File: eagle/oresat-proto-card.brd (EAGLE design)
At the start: 99.8 x 94.7 mm, 114 parts, among them J1 J-SAMTEC-TFM-110-X1-XXX-D-RA, J2 U.FL, J3 U.FL, J4 U.FL, J6 J-SAMTEC-TFM-120-X1-XXX-D-RA, J7 FTSH-105-XX-X-DV-K, Q1 DMP2240UDM, Q3 MOSFET-PCH-SOT23-6, Q4 MOSFET-PCH-SOT23-6, Q5 PMV45EN, Q6 PMV45EN, U2 TCAN330, U3 MAX7310ATE, U4 MAX4211CETE, U5 TPS62111RSA, U6 STM32F042K6, U7 MCP1703A, X1 16MHZ-2.5x2mm

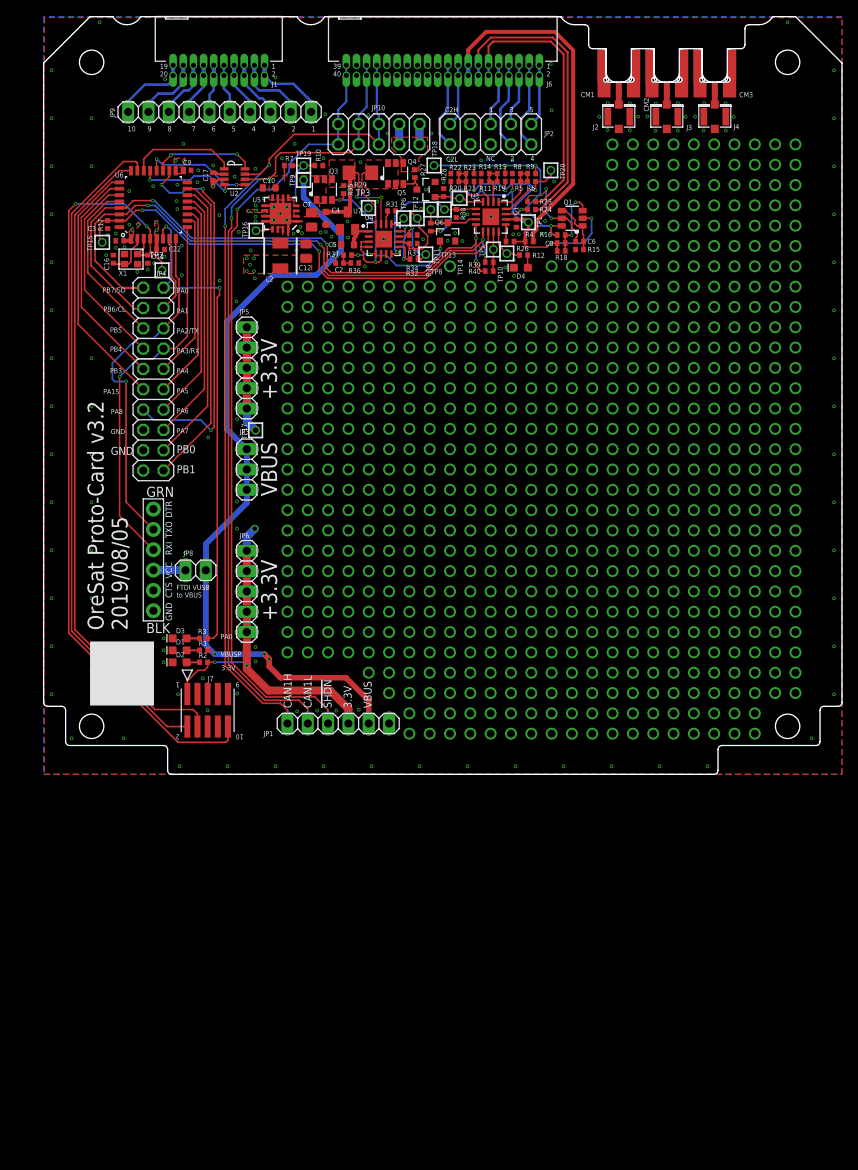
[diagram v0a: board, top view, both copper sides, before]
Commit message: updates to OPD, new I2C protection circuit
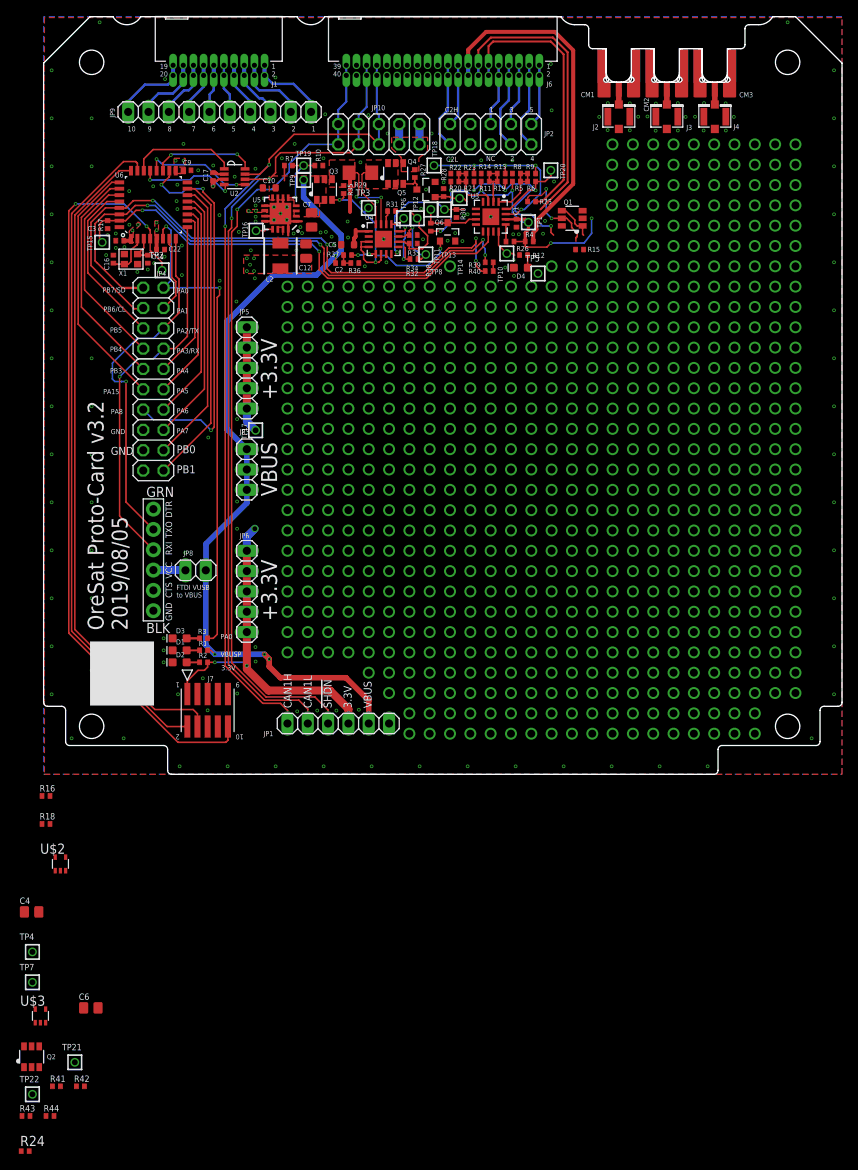
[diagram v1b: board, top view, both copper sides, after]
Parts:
- removed C8: TBD, rcl_custom:.0402-B-NOSILK
- removed U7: MCP1703A, v-reg:SOT23
- added Q2: DMP2240UDM, Q-MOSFET-PCH-dual-SOT23-6:SOT23-6
- added R41: 100, rcl_custom:.0402-B-NOSILK
- added R42: 10k, rcl_custom:.0402-B-NOSILK
- added R43, R44: NP, rcl_custom:.0402-B-NOSILK
- added TP21, TP22, TP4, TP7: TEST-POINT, Tova:2MM-TEST-POINT
- added U$2, U$3: MIC842, Q-Microchip-MIC842-Comparator:SC70-5
- C4: value 1u -> NP; device oresat-rcl:.0603-B-NOSILK -> oresat-rcl:.0805-B-NOSILK
- C6: value TBD -> NP; device rcl_custom:.0402-B-NOSILK -> oresat-rcl:.0805-B-NOSILK
- R16, R18: value 10k -> NP
- R24: value 100 -> 10k; device rcl_custom:.0402-B-NOSILK -> rcl:R0402
- moved R24 133.6 mm to (-2.30, -47.1), turned to 0 degrees
- moved C6 113.6 mm to (5.90, -29.2)
- moved R18 96.3 mm to (0.30, -6.20), turned to 0 degrees
- moved R16 95.2 mm to (0.30, -2.70)
- moved C4 94.2 mm to (-1.50, -17.2), turned to 0 degrees
- moved TP5 6.33 mm to (61.8, 62.6)
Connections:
- net BOOT renamed BOOT0
- removed net N$573: R12.2, TP10.1, U3.12
- removed net N$581: C8.2, Q1.3, R16.2, R18.1
- removed net N$598: R31.2, U4.14
- removed net N$600: TP6.1, U4.13
- removed net PA15: JP4.11, U6.25
- removed net PA8: JP4.13, U6.18
- new net IOUT: JP4.11, R31.2, U4.14, U6.25
- new net N$479: Q2.5, R41.2
- new net N$480: Q2.1, R42.2, TP22.1, U$3.5
- new net POUT: R24.1, TP6.1, U4.13
- new net POUTNAM: JP4.13, R24.2, U6.18
- net CB-RESET: now also U3.9, U4.9; no longer U3.5, U4.8
- net GND: now also C6.2, R42.1, U$2.2, U$3.2; no longer U7.1
- net MAX4211-3V3: now also TP10.1, U3.12; no longer U7.2
- net N$398: no longer C4.1, U7.3
- net N$579: no longer C6.1
- net N$580: now also TP7.1, U$2.5; no longer C6.2, Q1.4
- net N$599: now also U4.8; no longer U4.9
- net ON/!OFF: now also R12.2, U3.8; no longer U3.4
- net OPD_SCL: now also R41.1; no longer R24.1
- net PB6/SCL: now also U3.4; no longer U3.8
- net PB7/SDA: now also U3.5; no longer U3.9
- net PEN-SCL-FILT: now also C6.1, Q2.6, R43.1, R43.2, R44.1, TP21.1, U$3.1; no longer R24.2
- net PEN-SDA-FILT: now also C4.1, R16.2, R18.1, TP4.1, U$2.1
- net VPD: now also R44.2, U$2.4, U$3.4; no longer C8.1, Q1.2
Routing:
- net POUTNAM: track 0.00 -> 48.5 mm, vias 0 -> 3
- net PA8: track 48.5 -> 0.00 mm, vias 3 -> 0
- net IOUT: track 0.00 -> 33.6 mm
- net PA15: track 31.9 -> 0.00 mm
- net N$581: track 8.81 -> 0.00 mm, vias 2 -> 0
- net N$573: track 4.85 -> 0.00 mm
- net MAX4211-3V3: track 3.79 -> 7.65 mm
- net N$385: track 4.95 -> 1.14 mm
- net N$398: track 18.6 -> 15.6 mm
- net VPD: track 46.0 -> 43.1 mm
- net N$580: track 6.65 -> 4.40 mm
- net ON/!OFF: track 6.27 -> 4.28 mm
- net CB-RESET: track 16.7 -> 14.8 mm
- net POUT: track 0.00 -> 1.83 mm
- net N$600: track 1.83 -> 0.00 mm
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
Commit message: added board layout of new I2C protection circuit
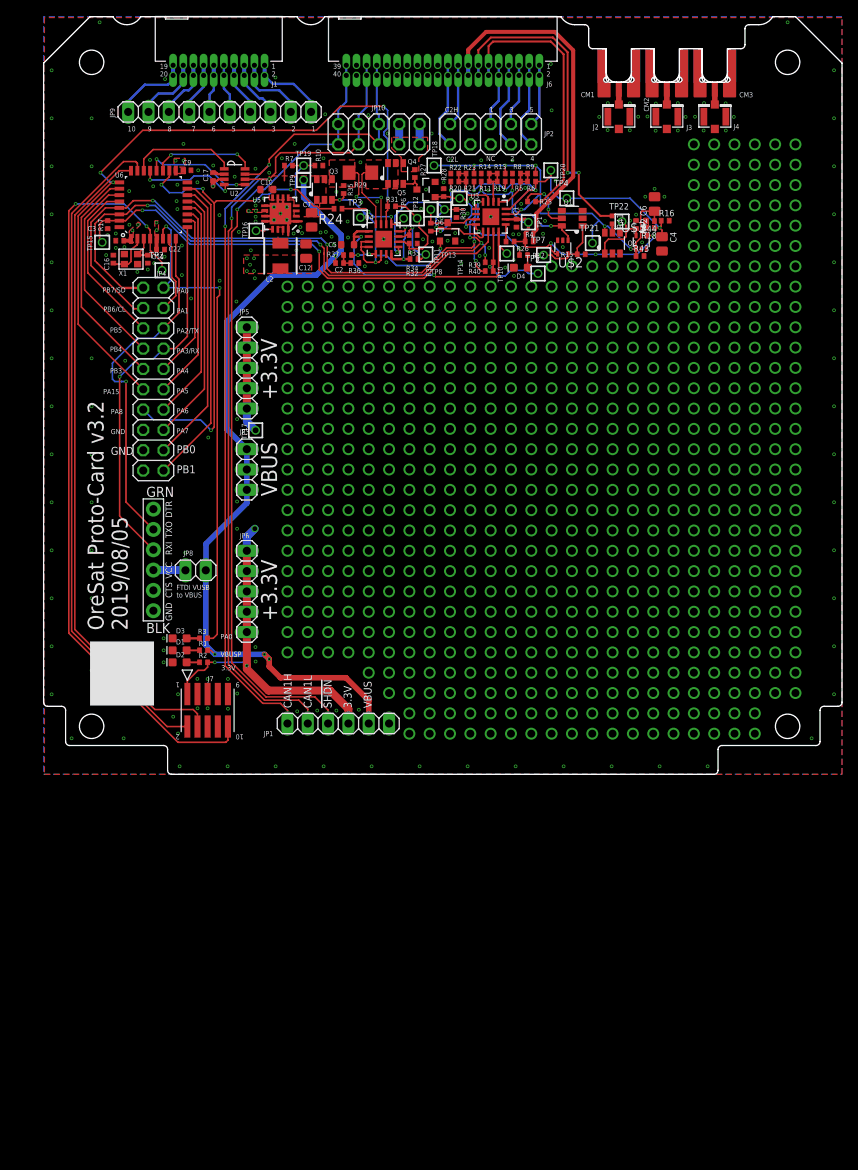
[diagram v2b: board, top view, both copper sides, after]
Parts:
- moved R44 134.7 mm to (75.8, 69.2), turned to 180 degrees
- moved R43 132.1 mm to (74.5, 64.8)
- moved TP22 131.7 mm to (72.3, 69.1)
- moved R41 128.7 mm to (71.1, 69.3), turned to 270 degrees
- moved R42 128.2 mm to (74.1, 68.7), turned to 270 degrees
- moved Q2 125.0 mm to (71.1, 66.4)
- moved R24 124.1 mm to (36.8, 70.7), turned to 180 degrees
- moved C6 122.7 mm to (76.4, 71.3), turned to 90 degrees
- moved U$3 122.4 mm to (74.7, 66.5)
- moved TP21 121.1 mm to (68.6, 66.4)
- moved TP4 115.5 mm to (65.4, 72.0)
- moved C4 114.8 mm to (77.3, 66.3), turned to 270 degrees
- moved TP7 111.1 mm to (62.5, 64.9)
- moved R18 106.1 mm to (75.8, 68.3), turned to 180 degrees
- moved R16 105.6 mm to (77.7, 69.2)
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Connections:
- net POUTNAM renamed POUTPROT
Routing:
- net IOUT: track 33.6 -> 88.3 mm, vias 0 -> 4
- net PEN-SCL-FILT: track 24.9 -> 53.9 mm, vias 4 -> 6
- net MAX4211-3V3: track 7.65 -> 35.4 mm, vias 0 -> 2
- net PEN-SDA-FILT: track 30.4 -> 53.8 mm, vias 4 -> 5
- net POUTPROT: track 48.5 -> 65.2 mm, vias 3 -> 5
- net ON/!OFF: track 4.28 -> 17.2 mm, vias 0 -> 4
- net N$385: track 1.14 -> 12.3 mm, vias 0 -> 1
- net CB-RESET: track 14.8 -> 24.8 mm, vias 1 -> 2
- net VPD: track 43.1 -> 52.5 mm, vias 6 -> 7
- net N$480: track 0.00 -> 8.94 mm
- net POUT: track 1.83 -> 9.34 mm, vias 0 -> 2
- net PB7/SDA: track 71.6 -> 78.1 mm, vias 4 -> 6
- net N$579: track 12.7 -> 7.44 mm
- net PB6/SCL: track 76.0 -> 80.9 mm, vias 4 -> 5
- net N$398: track 15.6 -> 10.7 mm
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- added copper zone on layer 1, net VPD

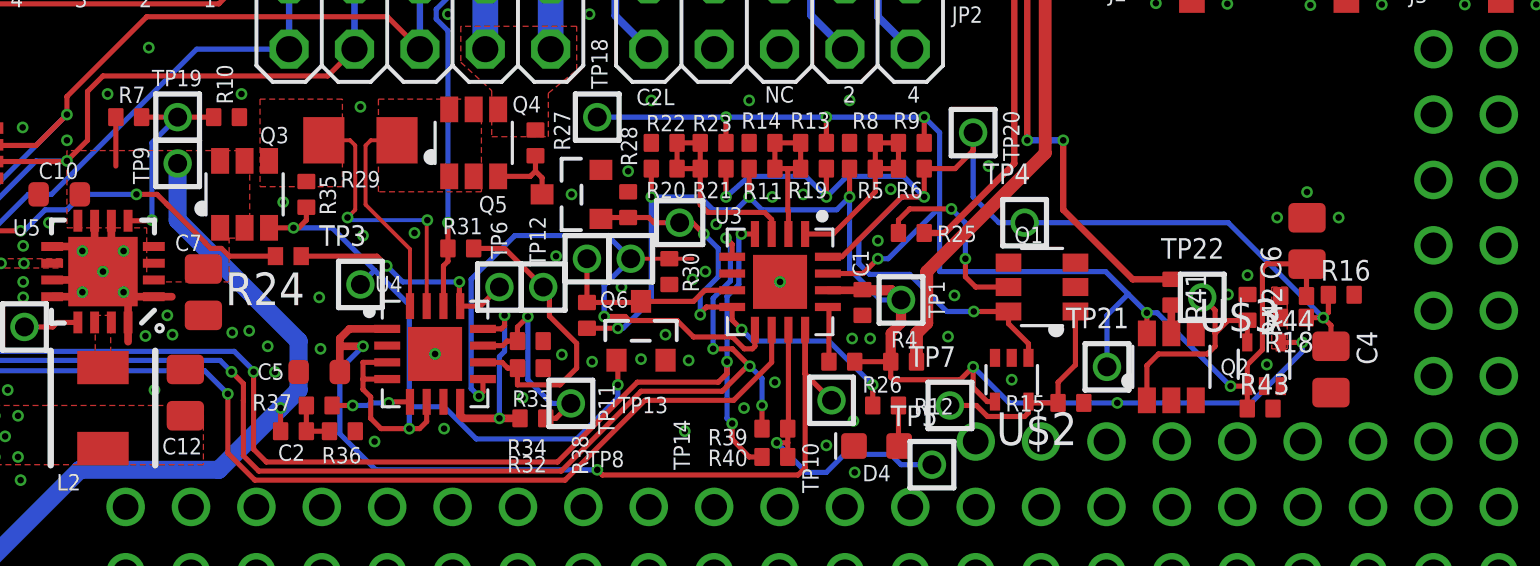
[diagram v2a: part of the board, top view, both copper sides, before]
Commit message: stray airwire
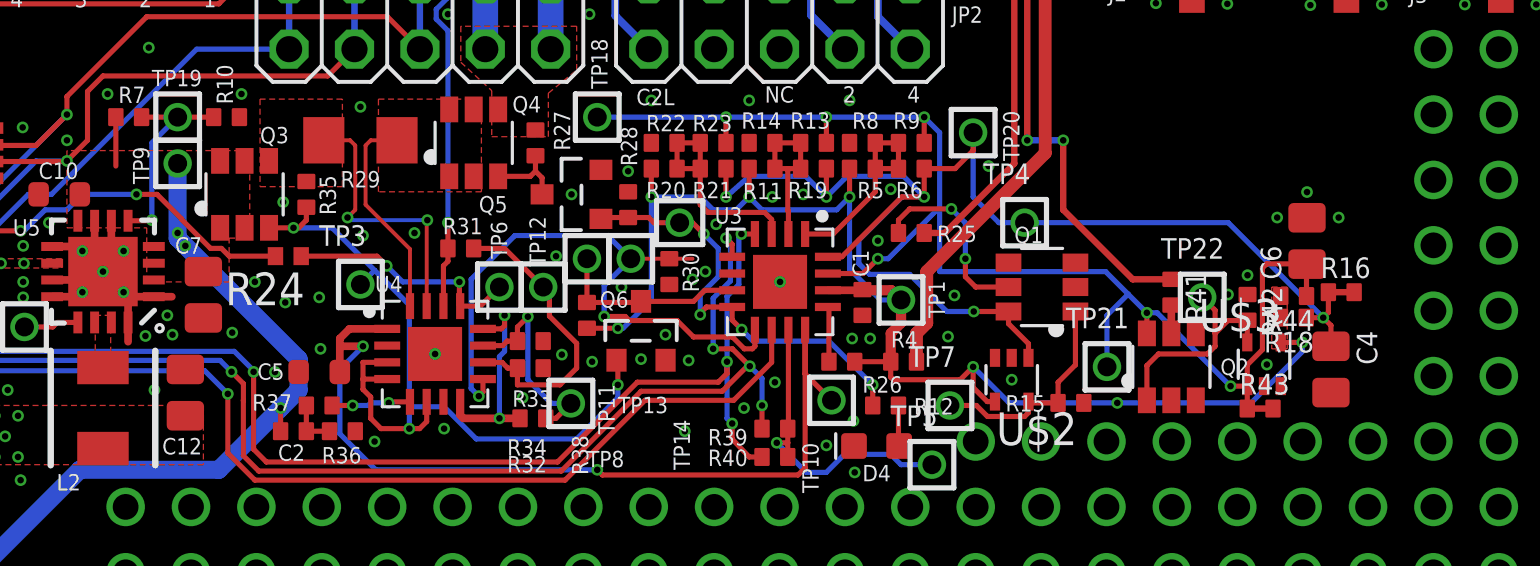
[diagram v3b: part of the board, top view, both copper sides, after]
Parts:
- moved C7 0.10 mm to (33.5, 69.2)
- moved R16 0.10 mm to (77.7, 69.3)
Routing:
- net PEN-SDA-FILT: track 53.8 -> 54.9 mm
- net PEN-SCL-FILT: track 53.9 -> 54.9 mm
- net VBUSP: vias 4 -> 6
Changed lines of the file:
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@@
 <attribute name="NAME" x="31.5" y="77.3" size="0.635" layer="25" font="vector" ratio="20"/>
 </element>
-<element name="C7" library="oresat-rcl" package=".0805-B-NOSILK" value="10u" x="33.5" y="69.3" smashed="yes" rot="R270">
-<attribute name="NAME" x="32.4" y="70.9" size="0.635" layer="25" font="vector" ratio="20"/>
-<attribute name="NAME" x="33.5" y="69.3" size="0.4" layer="33" ratio="15" rot="R270" align="center"/>
-<attribute name="VALUE" x="31.7" y="70.8" size="0.8" layer="27" font="vector" ratio="15" rot="R270"/>
+<element name="C7" library="oresat-rcl" package=".0805-B-NOSILK" value="10u" x="33.5" y="69.2" smashed="yes" rot="R270">
+<attribute name="NAME" x="32.4" y="70.8" size="0.635" layer="25" font="vector" ratio="20"/>
+<attribute name="NAME" x="33.5" y="69.2" size="0.4" layer="33" ratio="15" rot="R270" align="center"/>
+<attribute name="VALUE" x="31.7" y="70.7" size="0.8" layer="27" font="vector" ratio="15" rot="R270"/>
 </element>
 <element name="C10" library="oresat-rcl" package=".0603-B-NOSILK" value="1u" x="27.9" y="73.1" smashed="yes" rot="R180">
@@
 <attribute name="NAME" x="60.2" y="64.1" size="0.8" layer="25" font="vector" ratio="20"/>
 </element>
-<element name="R16" library="rcl_custom" package=".0402-B-NOSILK" value="NP" x="77.7" y="69.2" smashed="yes">
-<attribute name="DIS" value="Digi-Key" x="77.7" y="69.2" size="1.778" layer="27" display="off"/>
-<attribute name="DPN" value="1276-4275-1-ND" x="77.7" y="69.2" size="1.778" layer="27" display="off"/>
-<attribute name="MFR" value="Samsung" x="77.7" y="69.2" size="1.778" layer="27" display="off"/>
-<attribute name="MPN" value="RC1005F6653CS" x="77.7" y="69.2" size="1.778" layer="27" display="off"/>
-<attribute name="NAME" x="77.7" y="69.2" size="0.2" layer="33" ratio="15" align="center"/>
-<attribute name="NAME" x="76.9" y="69.75" size="0.8" layer="25" font="vector" ratio="15"/>
-<attribute name="VALUE" x="76.9" y="67.85" size="0.8" layer="27" font="vector" ratio="15"/>
+<element name="R16" library="rcl_custom" package=".0402-B-NOSILK" value="NP" x="77.7" y="69.3" smashed="yes">
+<attribute name="DIS" value="Digi-Key" x="77.7" y="69.3" size="1.778" layer="27" display="off"/>
+<attribute name="DPN" value="1276-4275-1-ND" x="77.7" y="69.3" size="1.778" layer="27" display="off"/>
+<attribute name="MFR" value="Samsung" x="77.7" y="69.3" size="1.778" layer="27" display="off"/>
+<attribute name="MPN" value="RC1005F6653CS" x="77.7" y="69.3" size="1.778" layer="27" display="off"/>
+<attribute name="NAME" x="77.7" y="69.3" size="0.2" layer="33" ratio="15" align="center"/>
+<attribute name="NAME" x="76.9" y="69.85" size="0.8" layer="25" font="vector" ratio="15"/>
+<attribute name="VALUE" x="76.9" y="67.95" size="0.8" layer="27" font="vector" ratio="15"/>
 </element>
 <element name="R18" library="rcl_custom" package=".0402-B-NOSILK" value="NP" x="75.84" y="68.31" smashed="yes" rot="R180">
@@
 <via x="59.4" y="67.5" extent="1-16" drill="0.254"/>
 <contactref element="C5" pad="2"/>
-<via x="35.28" y="67.8" extent="1-16" drill="0.254"/>
+<via x="36.68" y="68.9" extent="1-16" drill="0.254"/>
 <via x="36.28" y="66.2" extent="1-16" drill="0.254"/>
 <via x="40.15" y="63.5" extent="1-16" drill="0.254"/>
@@
 <via x="39.7" y="71.5" extent="1-16" drill="0.254"/>
 <via x="38" y="69.1" extent="1-16" drill="0.254"/>
-<via x="36" y="67.2" extent="1-16" drill="0.254"/>
+<via x="35.5" y="69.7" extent="1-16" drill="0.254"/>
 <via x="31.6" y="65.5" extent="1-16" drill="0.254"/>
 <via x="25.9" y="65.5" extent="1-16" drill="0.254"/>
@@
 <wire x1="36.3" y1="70.7" x2="34.5031375" y2="70.7" width="0.2" layer="1"/>
 <wire x1="34.5031375" y1="70.7" x2="34.2011375" y2="71.002" width="0.2" layer="1"/>
-<wire x1="33.573" y1="71.205975" x2="33.573" y2="71.227" width="0.2" layer="1"/>
-<wire x1="33.776975" y1="71.002" x2="33.573" y2="71.205975" width="0.2" layer="1"/>
 <wire x1="34.2011375" y1="71.002" x2="33.776975" y2="71.002" width="0.2" layer="1"/>
-<wire x1="33.573" y1="71.227" x2="32.15" y2="72.65" width="0.2" layer="1"/>
-<wire x1="32.15" y1="72.65" x2="32.073" y2="72.727" width="0.2" layer="1"/>
-<wire x1="32.073" y1="72.727" x2="31.7" y2="73.1" width="0.2" layer="1"/>
+<wire x1="33.776975" y1="71.002" x2="32.65" y2="72.128975" width="0.2" layer="1"/>
+<wire x1="32.65" y1="72.128975" x2="32.65" y2="72.15" width="0.2" layer="1"/>
+<wire x1="32.65" y1="72.15" x2="31.7" y2="73.1" width="0.2" layer="1"/>
 <wire x1="31.7" y1="73.1" x2="30.9" y2="73.1" width="0.2" layer="1"/>
 <via x="30.9" y="73.1" extent="1-16" drill="0.254"/>
@@
 <wire x1="30.1" y1="76.1" x2="30.1" y2="74.2" width="0.2" layer="1"/>
 <via x="36.5" y="64.8" extent="1-16" drill="0.254"/>
-<wire x1="32.5" y1="74.3" x2="32.5" y2="72.1" width="0.7" layer="16"/>
-<wire x1="32.5" y1="72.1" x2="37.2" y2="67.4" width="0.7" layer="16"/>
-<wire x1="37.2" y1="67.4" x2="37.2" y2="65.5" width="0.7" layer="16"/>
+<wire x1="32.5" y1="74.3" x2="32.5" y2="71.4" width="0.7" layer="16"/>
+<wire x1="32.5" y1="71.4" x2="37.2" y2="66.7" width="0.7" layer="16"/>
+<wire x1="37.2" y1="66.7" x2="37.2" y2="65.5" width="0.7" layer="16"/>
 <wire x1="37.2" y1="65.5" x2="36.5" y2="64.8" width="0.7" layer="16"/>
 <wire x1="36.5" y1="64.8" x2="34.1" y2="62.4" width="0.7" layer="16"/>
@@
 <via x="27.6" y="15" extent="1-16" drill="0.254"/>
 <wire x1="27.6" y1="15" x2="28.2" y2="14.4" width="0.7" layer="1"/>
-<wire x1="32.5" y1="72.1" x2="31.575" y2="71.075" width="0" layer="19" extent="1-16"/>
+<via x="32.5" y="71.6" extent="1-16" drill="0.254"/>
+<via x="32.8" y="71.1" extent="1-16" drill="0.254"/>
+<wire x1="32.5" y1="71.4" x2="32.5" y2="71.6" width="0" layer="19" extent="16-16"/>
 </signal>
 <signal name="VPD">
@@
 <wire x1="68.6" y1="66.4" x2="68.6" y2="68.4" width="0.2" layer="16"/>
 <wire x1="68.6" y1="68.4" x2="69.425" y2="69.225" width="0.2" layer="16"/>
-<wire x1="74.05" y1="64.78" x2="75.05" y2="64.78" width="0" layer="19" extent="1-1"/>
+<wire x1="75.05" y1="64.78" x2="74.05" y2="64.78" width="0.25" layer="1"/>
 </signal>
 <signal name="PEN-SDA-FILT">
@@
 <wire x1="77" y1="68.31" x2="77.3" y2="68.01" width="0.2" layer="1"/>
 <wire x1="77.3" y1="68.01" x2="77.3" y2="67.2" width="0.2" layer="1"/>
-<wire x1="77.2" y1="69.2" x2="77.2" y2="68.51" width="0.2" layer="1"/>
+<wire x1="77.2" y1="69.3" x2="77.2" y2="68.51" width="0.2" layer="1"/>
 <wire x1="77.2" y1="68.51" x2="77" y2="68.31" width="0.2" layer="1"/>
-<wire x1="77.2" y1="69.2" x2="78.2" y2="69.2" width="0" layer="19" extent="1-1"/>
+<wire x1="77.2" y1="69.3" x2="78.2" y2="69.3" width="0.25" layer="1"/>
 </signal>
 <signal name="POUT">
